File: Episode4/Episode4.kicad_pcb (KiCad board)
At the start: 2 copper layers, 175.3 x 181.6 mm, 64 parts, among them J1 BUS 1, J10 ATX POWER, J2 BUS 2, J3 BUS 3, J4 BUS 4, J5 BUS 5, J6 BUS 6, J7 BUS 7, J8 Conn_02x31_Top_Bottom, J9 Conn_02x18_Top_Bottom, SW1 POWER, U1 74HCT14, U2 74HCT74

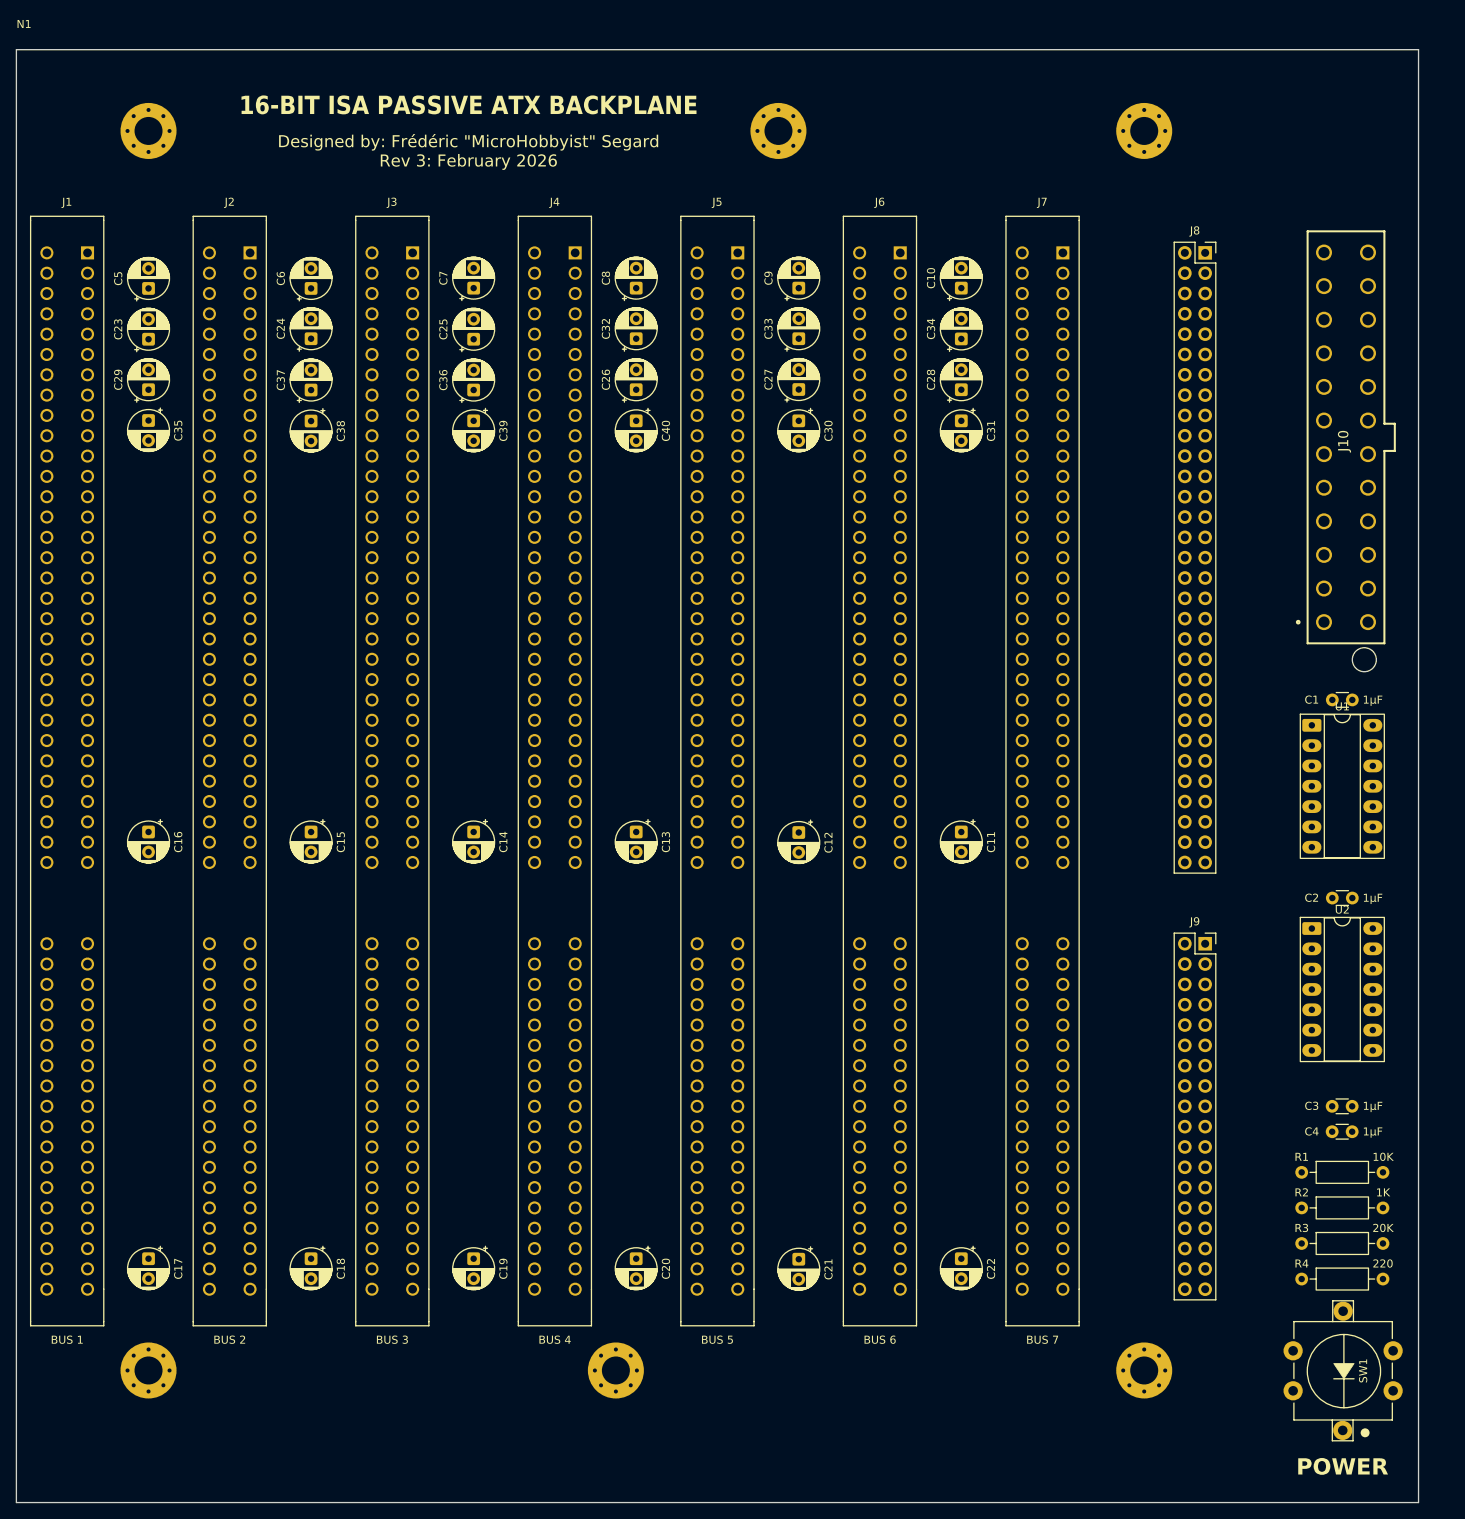
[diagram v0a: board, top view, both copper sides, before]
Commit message: Added traces to the backplane manually.
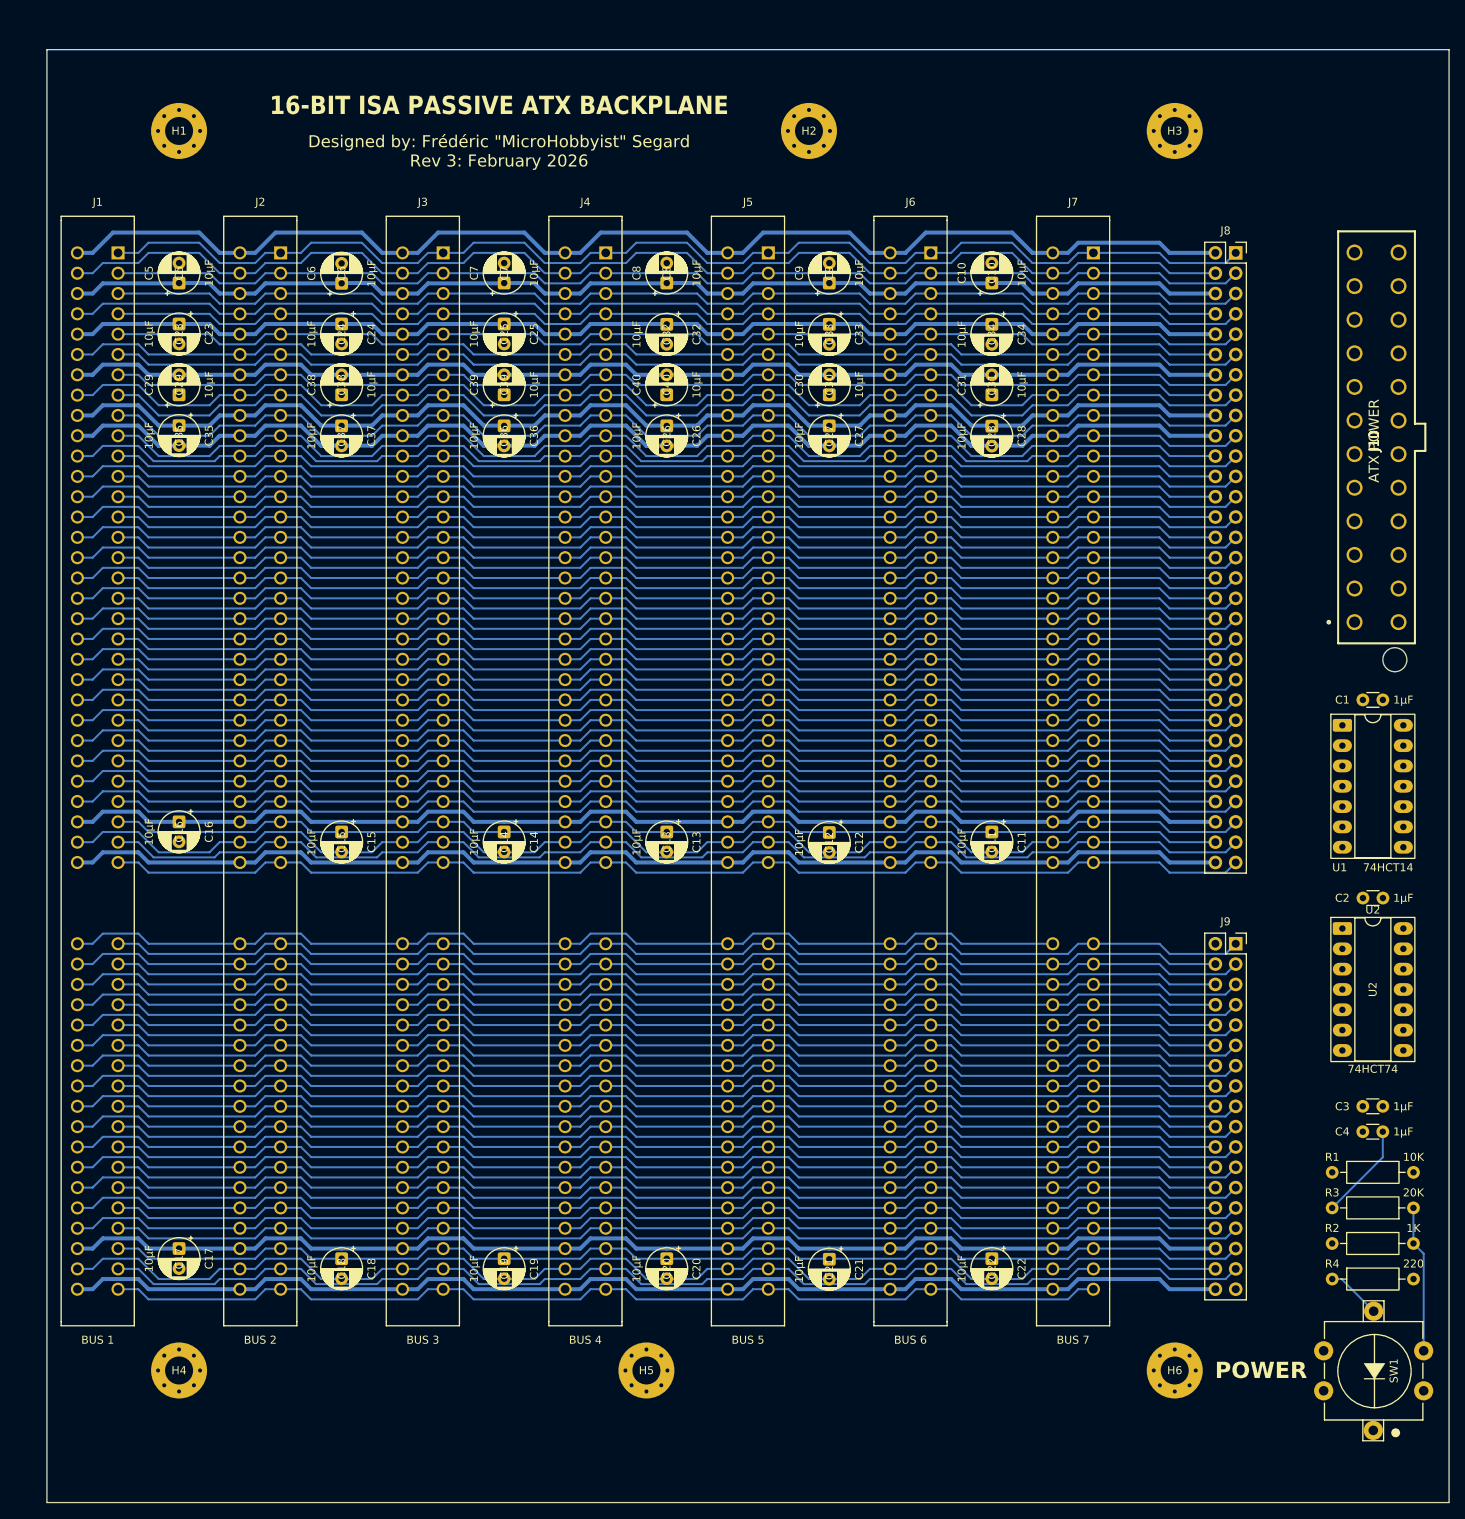
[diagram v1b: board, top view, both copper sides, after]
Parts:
- moved R3 14.7 mm to (200.0, 163.8), turned to 180 degrees
- moved C2 6.33 mm to (196.2, 125.1), turned to 180 degrees
- moved C3 6.33 mm to (196.2, 151.1), turned to 180 degrees
- moved C4 6.33 mm to (196.2, 154.3), turned to 180 degrees
- moved C27 5.93 mm to (127.0, 66.1), turned to -90 degrees
- moved C28 5.93 mm to (147.3, 66.1), turned to -90 degrees
- moved C26 5.92 mm to (106.7, 66.1), turned to -90 degrees
- moved C37 5.88 mm to (66.0, 66.1), turned to -90 degrees
- moved C36 5.88 mm to (86.4, 66.1), turned to -90 degrees
- moved R2 5.85 mm to (189.9, 168.3)
- moved C38 5.03 mm to (66.0, 62.2), turned to 90 degrees
- moved C31 5.02 mm to (147.3, 62.2), turned to 90 degrees
- moved C30 5.02 mm to (127.0, 62.2), turned to 90 degrees
- moved C39 5.02 mm to (86.4, 62.2), turned to 90 degrees
- moved C40 5.01 mm to (106.7, 62.2), turned to 90 degrees
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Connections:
- J1 pad 34: /+5V -> +5V
- J1 pad 36: /+3V3 -> +3V3
- J1 pad 38: /-12V -> -12V
- J1 pad 40: /+12V -> +12V
- J1 pad 60: /+5V -> +5V
- J1 pad 96: /+5V -> +5V
- J2 pad 34: /+5V -> +5V
- J2 pad 36: /+3V3 -> +3V3
- J2 pad 38: /-12V -> -12V
- J2 pad 40: /+12V -> +12V
- J2 pad 60: /+5V -> +5V
- J2 pad 96: /+5V -> +5V
- J3 pad 34: /+5V -> +5V
- J3 pad 36: /+3V3 -> +3V3
- J3 pad 38: /-12V -> -12V
- J3 pad 40: /+12V -> +12V
- J3 pad 60: /+5V -> +5V
- J3 pad 96: /+5V -> +5V
- J4 pad 34: /+5V -> +5V
- J4 pad 36: /+3V3 -> +3V3
- J4 pad 38: /-12V -> -12V
- J4 pad 40: /+12V -> +12V
- J4 pad 60: /+5V -> +5V
- J4 pad 96: /+5V -> +5V
- J5 pad 34: /+5V -> +5V
- J5 pad 36: /+3V3 -> +3V3
- J5 pad 38: /-12V -> -12V
- J5 pad 40: /+12V -> +12V
- J5 pad 60: /+5V -> +5V
- J5 pad 96: /+5V -> +5V
- J6 pad 34: /+5V -> +5V
- J6 pad 36: /+3V3 -> +3V3
- J6 pad 38: /-12V -> -12V
- J6 pad 40: /+12V -> +12V
- J6 pad 60: /+5V -> +5V
- J6 pad 96: /+5V -> +5V
- J7 pad 34: /+5V -> +5V
- J7 pad 36: /+3V3 -> +3V3
- J7 pad 38: /-12V -> -12V
- J7 pad 40: /+12V -> +12V
- J7 pad 60: /+5V -> +5V
- J7 pad 96: /+5V -> +5V
- J8 pad 10: /~{CBLK} -> +3V3
- J8 pad 11: /USR0 -> /D3
- J8 pad 12: /~{MREQ} -> /E
- J8 pad 13: /BA -> /D2
- J8 pad 14: /BS -> -12V
- J8 pad 15: /~{VMA} -> /D1
- J8 pad 16: /A15 -> /Q
- J8 pad 17: /A14 -> /D0
- J8 pad 18: /A13 -> +12V
- J8 pad 19: /A12 -> /~{CBLK}
- J8 pad 2: /D7 -> GND
- J8 pad 20: /A11 -> GND
- J8 pad 21: /A10 -> /USR0
- J8 pad 22: /A9 -> /~{WR}
- J8 pad 23: /A8 -> /~{MREQ}
- J8 pad 24: /A7 -> /~{RD}
- J8 pad 25: /A6 -> /BA
- J8 pad 26: /A5 -> /R/~{W}
- J8 pad 27: /A4 -> /BS
- J8 pad 28: /A3 -> /~{RAM_{oe}}
- J8 pad 29: /A2 -> /~{VMA}
- J8 pad 3: /D6 -> /D7
- J8 pad 30: /A1 -> /MMU_{en}
- J8 pad 31: /A0 -> /A15
- J8 pad 32: GND -> /~{MRDY}
- J8 pad 33: /RESET -> /A14
- J8 pad 34: /+5V -> /~{HALT}
- J8 pad 35: /~{RESET} -> /A13
- J8 pad 36: /+3V3 -> /~{BREQ}
- J8 pad 37: /E -> /A12
- J8 pad 38: /-12V -> /~{NMI}
- J8 pad 39: /Q -> /A11
- J8 pad 4: /D5 -> /RESET
- J8 pad 40: /+12V -> /CLK_{acia}
- J8 pad 41: GND -> /A10
- J8 pad 42: /~{WR} -> /~{IRQ7}
- J8 pad 43: /~{RD} -> /A9
- J8 pad 44: /R/~{W} -> /~{IRQ6}
- J8 pad 45: /~{RAM_{oe}} -> /A8
- J8 pad 46: /MMU_{en} -> /~{IRQ5}
- J8 pad 47: /~{MRDY} -> /A7
- J8 pad 48: /~{HALT} -> /~{IRQ4}
- J8 pad 49: /~{BREQ} -> /A6
- J8 pad 5: /D4 -> /D6
- J8 pad 50: /~{NMI} -> /~{IRQ3}
- J8 pad 51: /CLK_{acia} -> /A5
- J8 pad 52: /~{IRQ7} -> /~{IRQ2}
- J8 pad 53: /~{IRQ6} -> /A4
- J8 pad 54: /~{IRQ5} -> /~{IRQ1}
- J8 pad 55: /~{IRQ4} -> /A3
- J8 pad 56: /~{IRQ3} -> /~{IRQ0}
- J8 pad 57: /~{IRQ2} -> /A2
- J8 pad 58: /~{IRQ1} -> +5V
- J8 pad 59: /~{IRQ0} -> /A1
- J8 pad 6: /D3 -> +5V
- J8 pad 60: /+5V -> /CLK_{cpu}
- J8 pad 61: /CLK_{cpu} -> /A0
- J8 pad 7: /D2 -> /D5
- J8 pad 8: /D1 -> /~{RESET}
- J8 pad 9: /D0 -> /D4
- J9 pad 10: /CLK_{2} -> /~{IRQ12}
- J9 pad 11: /D8 -> /A19
- J9 pad 12: /D9 -> /~{IRQ13}
- J9 pad 13: /D10 -> /A18
- J9 pad 14: /D11 -> /~{IRQ14}
- J9 pad 15: /D12 -> /A17
- J9 pad 16: /D13 -> /~{IRQ15}
- J9 pad 17: /D14 -> /A16
- J9 pad 18: /D15 -> /USR1
- J9 pad 19: /~{IRQ8} -> /CLK_{2}
- J9 pad 2: /A23 -> /~{IRQ8}
- J9 pad 20: /~{IRQ9} -> /USR2
- J9 pad 21: /~{IRQ10} -> /D8
- J9 pad 22: /~{IRQ11} -> /USR3
- J9 pad 23: /~{IRQ12} -> /D9
- J9 pad 24: /~{IRQ13} -> /USR4
- J9 pad 25: /~{IRQ14} -> /D10
- J9 pad 26: /~{IRQ15} -> /USR5
- J9 pad 27: /USR1 -> /D11
- J9 pad 28: /USR2 -> /USR6
- J9 pad 29: /USR3 -> /D12
- J9 pad 3: /A22 -> /A23
- J9 pad 30: /USR4 -> /USR7
- J9 pad 31: /USR5 -> /D13
- J9 pad 32: /USR6 -> +5V
- J9 pad 33: /USR7 -> /D14
- J9 pad 34: /+5V -> /USR8
- J9 pad 35: /USR8 -> /D15
- J9 pad 4: /A21 -> /~{IRQ9}
- J9 pad 5: /A20 -> /A22
- J9 pad 6: /A19 -> /~{IRQ10}
- J9 pad 7: /A18 -> /A21
- J9 pad 8: /A17 -> /~{IRQ11}
- J9 pad 9: /A16 -> /A20
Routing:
- net GND: track 0.00 -> 611.3 mm
- net +5V: track 0.00 -> 449.2 mm
- net /D2: track 0.00 -> 203.6 mm
- net /Q: track 0.00 -> 198.7 mm
- net /RESET: track 0.00 -> 155.9 mm
- net +12V: track 0.00 -> 155.9 mm
- net /D0: track 0.00 -> 153.4 mm
- net /D1: track 0.00 -> 153.4 mm
- net /~{IORQ}: track 0.00 -> 153.4 mm
- net /~{CBLK}: track 0.00 -> 153.4 mm
- net /~{WR}: track 0.00 -> 152.8 mm
- net /D14: track 0.00 -> 150.2 mm
- net /~{IRQ15}: track 0.00 -> 149.6 mm
- net /~{IRQ14}: track 0.00 -> 149.6 mm
- net /~{IRQ12}: track 0.00 -> 149.6 mm
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
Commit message: Added more capacitors and extended the bus form 7 to 12
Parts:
- removed N1: Housing, MicroHobbyist:ATX_Backplane
- added C100: .1µF, Capacitor_THT:C_Disc_D3.4mm_W2.1mm_P2.50mm, F.Cu at (188.3, 170.7)
- added C101: .1µF, Capacitor_THT:C_Disc_D3.4mm_W2.1mm_P2.50mm, F.Cu at (188.3, 174.3)
- added C102: .1µF, Capacitor_THT:C_Disc_D3.4mm_W2.1mm_P2.50mm, F.Cu at (188.3, 178.0)
- added C103: .1µF, Capacitor_THT:C_Disc_D3.4mm_W2.1mm_P2.50mm, F.Cu at (188.3, 181.6)
- added C104: .1µF, Capacitor_THT:C_Disc_D3.4mm_W2.1mm_P2.50mm, F.Cu at (188.3, 185.3)
- added C105: .1µF, Capacitor_THT:C_Disc_D3.4mm_W2.1mm_P2.50mm, F.Cu at (188.3, 188.9)
- added C106: .1µF, Capacitor_THT:C_Disc_D3.4mm_W2.1mm_P2.50mm, F.Cu at (188.3, 192.6)
- added C107: .1µF, Capacitor_THT:C_Disc_D3.4mm_W2.1mm_P2.50mm, F.Cu at (188.3, 196.2)
- added C108: .1µF, Capacitor_THT:C_Disc_D3.4mm_W2.1mm_P2.50mm, F.Cu at (188.3, 199.9)
- added C109: .1µF, Capacitor_THT:C_Disc_D3.4mm_W2.1mm_P2.50mm, F.Cu at (193.9, 152.4)
- added C110: .1µF, Capacitor_THT:C_Disc_D3.4mm_W2.1mm_P2.50mm, F.Cu at (193.9, 156.1)
- added C111: .1µF, Capacitor_THT:C_Disc_D3.4mm_W2.1mm_P2.50mm, F.Cu at (193.9, 159.7)
- added C112: .1µF, Capacitor_THT:C_Disc_D3.4mm_W2.1mm_P2.50mm, F.Cu at (193.9, 163.4)
- added C113: .1µF, Capacitor_THT:C_Disc_D3.4mm_W2.1mm_P2.50mm, F.Cu at (193.9, 167.0)
- added C114: .1µF, Capacitor_THT:C_Disc_D3.4mm_W2.1mm_P2.50mm, F.Cu at (193.9, 170.7)
- added C115: .1µF, Capacitor_THT:C_Disc_D3.4mm_W2.1mm_P2.50mm, F.Cu at (193.9, 174.3)
- added C116: .1µF, Capacitor_THT:C_Disc_D3.4mm_W2.1mm_P2.50mm, F.Cu at (193.9, 178.0)
- added C117: .1µF, Capacitor_THT:C_Disc_D3.4mm_W2.1mm_P2.50mm, F.Cu at (193.9, 181.6)
- added C118: .1µF, Capacitor_THT:C_Disc_D3.4mm_W2.1mm_P2.50mm, F.Cu at (193.9, 185.3)
- added C119: .1µF, Capacitor_THT:C_Disc_D3.4mm_W2.1mm_P2.50mm, F.Cu at (193.9, 188.9)
- added C120: .1µF, Capacitor_THT:C_Disc_D3.4mm_W2.1mm_P2.50mm, F.Cu at (193.9, 192.6)
- added C121: .1µF, Capacitor_THT:C_Disc_D3.4mm_W2.1mm_P2.50mm, F.Cu at (193.9, 196.2)
- added C122: .1µF, Capacitor_THT:C_Disc_D3.4mm_W2.1mm_P2.50mm, F.Cu at (193.9, 199.9)
- added C123: .1µF, Capacitor_THT:C_Disc_D3.4mm_W2.1mm_P2.50mm, F.Cu at (199.6, 152.4)
- added C124: .1µF, Capacitor_THT:C_Disc_D3.4mm_W2.1mm_P2.50mm, F.Cu at (199.6, 156.1)
- added C125: .1µF, Capacitor_THT:C_Disc_D3.4mm_W2.1mm_P2.50mm, F.Cu at (199.6, 159.7)
- added C126: .1µF, Capacitor_THT:C_Disc_D3.4mm_W2.1mm_P2.50mm, F.Cu at (199.6, 163.4)
- added C127: .1µF, Capacitor_THT:C_Disc_D3.4mm_W2.1mm_P2.50mm, F.Cu at (199.6, 167.0)
- added C128: .1µF, Capacitor_THT:C_Disc_D3.4mm_W2.1mm_P2.50mm, F.Cu at (199.6, 170.7)
- added C129: .1µF, Capacitor_THT:C_Disc_D3.4mm_W2.1mm_P2.50mm, F.Cu at (199.6, 174.3)
- added C130: .1µF, Capacitor_THT:C_Disc_D3.4mm_W2.1mm_P2.50mm, F.Cu at (199.6, 178.0)
- added C131: 1µF, Capacitor_THT:C_Disc_D3.4mm_W2.1mm_P2.50mm, F.Cu at (199.6, 181.6)
- added C132: 1µF, Capacitor_THT:C_Disc_D3.4mm_W2.1mm_P2.50mm, F.Cu at (199.6, 185.3)
- added C133: 1µF, Capacitor_THT:C_Disc_D3.4mm_W2.1mm_P2.50mm, F.Cu at (199.6, 188.9)
- added C134: 1µF, Capacitor_THT:C_Disc_D3.4mm_W2.1mm_P2.50mm, F.Cu at (199.6, 192.6)
- added C135: 1µF, Capacitor_THT:C_Disc_D3.4mm_W2.1mm_P2.50mm, F.Cu at (199.6, 196.2)
- added C136: 1µF, Capacitor_THT:C_Disc_D3.4mm_W2.1mm_P2.50mm, F.Cu at (199.6, 199.9)
- added C137: 1µF, Capacitor_THT:C_Disc_D3.4mm_W2.1mm_P2.50mm, F.Cu at (205.2, 152.4)
- added C138: 1µF, Capacitor_THT:C_Disc_D3.4mm_W2.1mm_P2.50mm, F.Cu at (205.2, 156.1)
- added C139: 1µF, Capacitor_THT:C_Disc_D3.4mm_W2.1mm_P2.50mm, F.Cu at (205.2, 159.7)
- added C140: 1µF, Capacitor_THT:C_Disc_D3.4mm_W2.1mm_P2.50mm, F.Cu at (205.2, 163.4)
- added C141: 1µF, Capacitor_THT:C_Disc_D3.4mm_W2.1mm_P2.50mm, F.Cu at (205.2, 167.0)
- added C142: .1µF, Capacitor_THT:C_Disc_D3.4mm_W2.1mm_P2.50mm, F.Cu at (205.2, 170.7)
- added C143: .1µF, Capacitor_THT:C_Disc_D3.4mm_W2.1mm_P2.50mm, F.Cu at (205.2, 174.3)
- added C144: .1µF, Capacitor_THT:C_Disc_D3.4mm_W2.1mm_P2.50mm, F.Cu at (205.2, 178.0)
- added C145: .1µF, Capacitor_THT:C_Disc_D3.4mm_W2.1mm_P2.50mm, F.Cu at (205.2, 181.6)
- added C146: .1µF, Capacitor_THT:C_Disc_D3.4mm_W2.1mm_P2.50mm, F.Cu at (205.2, 185.3)
- added C147: .1µF, Capacitor_THT:C_Disc_D3.4mm_W2.1mm_P2.50mm, F.Cu at (205.2, 188.9)
- added C148: .1µF, Capacitor_THT:C_Disc_D3.4mm_W2.1mm_P2.50mm, F.Cu at (205.2, 192.6)
- added C149: .1µF, Capacitor_THT:C_Disc_D3.4mm_W2.1mm_P2.50mm, F.Cu at (205.2, 196.2)
- added C150: .1µF, Capacitor_THT:C_Disc_D3.4mm_W2.1mm_P2.50mm, F.Cu at (205.2, 199.9)
- added C151: .1µF, Capacitor_THT:C_Disc_D3.4mm_W2.1mm_P2.50mm, F.Cu at (210.9, 152.4)
- added C152: .1µF, Capacitor_THT:C_Disc_D3.4mm_W2.1mm_P2.50mm, F.Cu at (210.9, 156.1)
- added C153: 1µF, Capacitor_THT:C_Disc_D3.4mm_W2.1mm_P2.50mm, F.Cu at (210.9, 159.7)
- added C154: 1µF, Capacitor_THT:C_Disc_D3.4mm_W2.1mm_P2.50mm, F.Cu at (210.9, 163.4)
- added C155: 1µF, Capacitor_THT:C_Disc_D3.4mm_W2.1mm_P2.50mm, F.Cu at (210.9, 167.0)
- added C156: 1µF, Capacitor_THT:C_Disc_D3.4mm_W2.1mm_P2.50mm, F.Cu at (210.9, 170.7)
- added C157: 1µF, Capacitor_THT:C_Disc_D3.4mm_W2.1mm_P2.50mm, F.Cu at (210.9, 174.3)
- added C158: 1µF, Capacitor_THT:C_Disc_D3.4mm_W2.1mm_P2.50mm, F.Cu at (210.9, 178.0)
- added C159: 1µF, Capacitor_THT:C_Disc_D3.4mm_W2.1mm_P2.50mm, F.Cu at (210.9, 181.6)
- added C160: 1µF, Capacitor_THT:C_Disc_D3.4mm_W2.1mm_P2.50mm, F.Cu at (210.9, 185.3)
- added C161: 1µF, Capacitor_THT:C_Disc_D3.4mm_W2.1mm_P2.50mm, F.Cu at (210.9, 188.9)
- added C162: 1µF, Capacitor_THT:C_Disc_D3.4mm_W2.1mm_P2.50mm, F.Cu at (210.9, 192.6)
- added C163: 1µF, Capacitor_THT:C_Disc_D3.4mm_W2.1mm_P2.50mm, F.Cu at (210.9, 196.2)
- added C164: .1µF, Capacitor_THT:C_Disc_D3.4mm_W2.1mm_P2.50mm, F.Cu at (210.9, 199.9)
- added C165: .1µF, Capacitor_THT:C_Disc_D3.4mm_W2.1mm_P2.50mm, F.Cu at (216.5, 152.4)
- added C166: .1µF, Capacitor_THT:C_Disc_D3.4mm_W2.1mm_P2.50mm, F.Cu at (216.5, 156.1)
- added C167: .1µF, Capacitor_THT:C_Disc_D3.4mm_W2.1mm_P2.50mm, F.Cu at (216.5, 159.7)
- added C168: .1µF, Capacitor_THT:C_Disc_D3.4mm_W2.1mm_P2.50mm, F.Cu at (216.5, 163.4)
- added C169: .1µF, Capacitor_THT:C_Disc_D3.4mm_W2.1mm_P2.50mm, F.Cu at (216.5, 167.0)
- added C170: .1µF, Capacitor_THT:C_Disc_D3.4mm_W2.1mm_P2.50mm, F.Cu at (216.5, 170.7)
- added C171: .1µF, Capacitor_THT:C_Disc_D3.4mm_W2.1mm_P2.50mm, F.Cu at (216.5, 174.3)
- added C172: .1µF, Capacitor_THT:C_Disc_D3.4mm_W2.1mm_P2.50mm, F.Cu at (216.5, 178.0)
- added C173: .1µF, Capacitor_THT:C_Disc_D3.4mm_W2.1mm_P2.50mm, F.Cu at (216.5, 181.6)
- added C174: .1µF, Capacitor_THT:C_Disc_D3.4mm_W2.1mm_P2.50mm, F.Cu at (216.5, 185.3)
- added C41: 10µF, Capacitor_THT:CP_Radial_D5.0mm_P2.50mm, F.Cu at (145.3, 180.1)
- added C42: 10µF, Capacitor_THT:CP_Radial_D5.0mm_P2.50mm, F.Cu at (145.3, 186.6)
- added C43: 10µF, Capacitor_THT:CP_Radial_D5.0mm_P2.50mm, F.Cu at (145.3, 193.2)
- added C44: 10µF, Capacitor_THT:CP_Radial_D5.0mm_P2.50mm, F.Cu at (145.3, 199.7)
- added C45: 10µF, Capacitor_THT:CP_Radial_D5.0mm_P2.50mm, F.Cu at (151.9, 153.9)
- added C46: 10µF, Capacitor_THT:CP_Radial_D5.0mm_P2.50mm, F.Cu at (151.9, 160.4)
- added C47: 10µF, Capacitor_THT:CP_Radial_D5.0mm_P2.50mm, F.Cu at (151.9, 167.0)
- added C48: 10µF, Capacitor_THT:CP_Radial_D5.0mm_P2.50mm, F.Cu at (151.9, 173.5)
- added C49: 10µF, Capacitor_THT:CP_Radial_D5.0mm_P2.50mm, F.Cu at (151.9, 180.1)
- added C50: 10µF, Capacitor_THT:CP_Radial_D5.0mm_P2.50mm, F.Cu at (151.9, 186.6)
- added C51: 10µF, Capacitor_THT:CP_Radial_D5.0mm_P2.50mm, F.Cu at (151.9, 193.2)
- added C52: 10µF, Capacitor_THT:CP_Radial_D5.0mm_P2.50mm, F.Cu at (151.9, 199.7)
- added C53: 10µF, Capacitor_THT:CP_Radial_D5.0mm_P2.50mm, F.Cu at (158.6, 153.9)
- added C54: 10µF, Capacitor_THT:CP_Radial_D5.0mm_P2.50mm, F.Cu at (158.6, 160.4)
- added C55: 10µF, Capacitor_THT:CP_Radial_D5.0mm_P2.50mm, F.Cu at (158.6, 167.0)
- added C56: 10µF, Capacitor_THT:CP_Radial_D5.0mm_P2.50mm, F.Cu at (158.6, 173.5)
- added C57: 10µF, Capacitor_THT:CP_Radial_D5.0mm_P2.50mm, F.Cu at (158.6, 180.1)
- added C58: 10µF, Capacitor_THT:CP_Radial_D5.0mm_P2.50mm, F.Cu at (158.6, 186.6)
- added C59: 10µF, Capacitor_THT:CP_Radial_D5.0mm_P2.50mm, F.Cu at (158.6, 193.2)
- added C60: 10µF, Capacitor_THT:CP_Radial_D5.0mm_P2.50mm, F.Cu at (158.6, 199.7)
- added C61: 10µF, Capacitor_THT:CP_Radial_D5.0mm_P2.50mm, F.Cu at (165.2, 153.9)
- added C62: 10µF, Capacitor_THT:CP_Radial_D5.0mm_P2.50mm, F.Cu at (165.2, 160.4)
- added C63: 10µF, Capacitor_THT:CP_Radial_D5.0mm_P2.50mm, F.Cu at (165.2, 167.0)
- added C64: 10µF, Capacitor_THT:CP_Radial_D5.0mm_P2.50mm, F.Cu at (165.2, 173.5)
- added C65: 1µF, Capacitor_THT:C_Disc_D3.4mm_W2.1mm_P2.50mm, F.Cu at (171.3, 196.2)
- added C66: 1µF, Capacitor_THT:C_Disc_D3.4mm_W2.1mm_P2.50mm, F.Cu at (171.3, 199.9)
- added C67: 1µF, Capacitor_THT:C_Disc_D3.4mm_W2.1mm_P2.50mm, F.Cu at (177.0, 152.4)
- added C68: 1µF, Capacitor_THT:C_Disc_D3.4mm_W2.1mm_P2.50mm, F.Cu at (177.0, 156.1)
- added C69: 1µF, Capacitor_THT:C_Disc_D3.4mm_W2.1mm_P2.50mm, F.Cu at (177.0, 159.7)
- added C70: 1µF, Capacitor_THT:C_Disc_D3.4mm_W2.1mm_P2.50mm, F.Cu at (177.0, 163.4)
- added C71: 1µF, Capacitor_THT:C_Disc_D3.4mm_W2.1mm_P2.50mm, F.Cu at (177.0, 167.0)
- added C72: 1µF, Capacitor_THT:C_Disc_D3.4mm_W2.1mm_P2.50mm, F.Cu at (177.0, 170.7)
- added C73: 1µF, Capacitor_THT:C_Disc_D3.4mm_W2.1mm_P2.50mm, F.Cu at (177.0, 174.3)
- added C74: 1µF, Capacitor_THT:C_Disc_D3.4mm_W2.1mm_P2.50mm, F.Cu at (177.0, 178.0)
- added C75: 1µF, Capacitor_THT:C_Disc_D3.4mm_W2.1mm_P2.50mm, F.Cu at (177.0, 181.6)
- added C76: 1µF, Capacitor_THT:C_Disc_D3.4mm_W2.1mm_P2.50mm, F.Cu at (177.0, 185.3)
- added C77: 1µF, Capacitor_THT:C_Disc_D3.4mm_W2.1mm_P2.50mm, F.Cu at (177.0, 188.9)
- added C78: 1µF, Capacitor_THT:C_Disc_D3.4mm_W2.1mm_P2.50mm, F.Cu at (177.0, 192.6)
- added C79: 1µF, Capacitor_THT:C_Disc_D3.4mm_W2.1mm_P2.50mm, F.Cu at (177.0, 196.2)
- added C80: 1µF, Capacitor_THT:C_Disc_D3.4mm_W2.1mm_P2.50mm, F.Cu at (177.0, 199.9)
- added C81: 1µF, Capacitor_THT:C_Disc_D3.4mm_W2.1mm_P2.50mm, F.Cu at (182.6, 152.4)
- added C82: 1µF, Capacitor_THT:C_Disc_D3.4mm_W2.1mm_P2.50mm, F.Cu at (182.6, 156.1)
- added C83: 1µF, Capacitor_THT:C_Disc_D3.4mm_W2.1mm_P2.50mm, F.Cu at (182.6, 159.7)
- added C84: 1µF, Capacitor_THT:C_Disc_D3.4mm_W2.1mm_P2.50mm, F.Cu at (182.6, 163.4)
- added C85: 1µF, Capacitor_THT:C_Disc_D3.4mm_W2.1mm_P2.50mm, F.Cu at (182.6, 167.0)
- added C86: 1µF, Capacitor_THT:C_Disc_D3.4mm_W2.1mm_P2.50mm, F.Cu at (182.6, 170.7)
- added C87: 1µF, Capacitor_THT:C_Disc_D3.4mm_W2.1mm_P2.50mm, F.Cu at (182.6, 174.3)
- added C88: 1µF, Capacitor_THT:C_Disc_D3.4mm_W2.1mm_P2.50mm, F.Cu at (182.6, 178.0)
- added C89: 1µF, Capacitor_THT:C_Disc_D3.4mm_W2.1mm_P2.50mm, F.Cu at (182.6, 181.6)
- added C90: 1µF, Capacitor_THT:C_Disc_D3.4mm_W2.1mm_P2.50mm, F.Cu at (182.6, 185.3)
- added C91: 1µF, Capacitor_THT:C_Disc_D3.4mm_W2.1mm_P2.50mm, F.Cu at (182.6, 188.9)
- added C92: 1µF, Capacitor_THT:C_Disc_D3.4mm_W2.1mm_P2.50mm, F.Cu at (182.6, 192.6)
- added C93: 1µF, Capacitor_THT:C_Disc_D3.4mm_W2.1mm_P2.50mm, F.Cu at (182.6, 196.2)
- added C94: 1µF, Capacitor_THT:C_Disc_D3.4mm_W2.1mm_P2.50mm, F.Cu at (182.6, 199.9)
- added C95: 1µF, Capacitor_THT:C_Disc_D3.4mm_W2.1mm_P2.50mm, F.Cu at (188.3, 152.4)
- added C96: 1µF, Capacitor_THT:C_Disc_D3.4mm_W2.1mm_P2.50mm, F.Cu at (188.3, 156.1)
- added C97: 1µF, Capacitor_THT:C_Disc_D3.4mm_W2.1mm_P2.50mm, F.Cu at (188.3, 159.7)
- added C98: .1µF, Capacitor_THT:C_Disc_D3.4mm_W2.1mm_P2.50mm, F.Cu at (188.3, 163.4)
- added C99: .1µF, Capacitor_THT:C_Disc_D3.4mm_W2.1mm_P2.50mm, F.Cu at (188.3, 167.0)
- added H10: MH, MountingHole:MountingHole_3.5mm_Pad_Via, F.Cu at (94.0, 31.8)
- added H7: MH, MountingHole:MountingHole_3.5mm_Pad_Via, F.Cu at (276.9, 31.8)
- added H8: MH, MountingHole:MountingHole_3.5mm_Pad_Via, F.Cu at (215.9, 31.8)
- added H9: MH, MountingHole:MountingHole_3.5mm_Pad_Via, F.Cu at (154.9, 31.8)
- added J10: BUS 10, MicroHobbyist:ISA_Connector, F.Cu at (238.8, 44.5)
- added J11: BUS 11, MicroHobbyist:ISA_Connector, F.Cu at (259.1, 44.5)
- added J12: BUS 12, MicroHobbyist:ISA_Connector, F.Cu at (279.4, 44.5)
- added J8: BUS 8, MicroHobbyist:ISA_Connector, F.Cu at (198.1, 44.5)
- C1: renamed from C3; footprint Capacitor_THT:C_Disc_D3.0mm_W1.6mm_P2.50mm -> Capacitor_THT:C_Disc_D3.4mm_W2.1mm_P2.50mm
- C10, C13, C14, C17, C20, C7, C8, C9: value 10µF -> .1µF; footprint Capacitor_THT:CP_Radial_D5.0mm_P2.50mm -> Capacitor_THT:C_Disc_D3.4mm_W2.1mm_P2.50mm
- C11, C15, C18, C5: value 10µF -> 100µF; footprint Capacitor_THT:CP_Radial_D5.0mm_P2.50mm -> Capacitor_THT:CP_Radial_D6.3mm_P2.50mm
- C12, C16, C19, C6: value 10µF -> 1µF; footprint Capacitor_THT:CP_Radial_D5.0mm_P2.50mm -> Capacitor_THT:C_Disc_D3.4mm_W2.1mm_P2.50mm
- C2: renamed from C4; footprint Capacitor_THT:C_Disc_D3.0mm_W1.6mm_P2.50mm -> Capacitor_THT:C_Disc_D3.4mm_W2.1mm_P2.50mm
- C3: renamed from C1; value 1µF -> .1µF; footprint Capacitor_THT:C_Disc_D3.0mm_W1.6mm_P2.50mm -> Capacitor_THT:C_Disc_D3.4mm_W2.1mm_P2.50mm
- C4: renamed from C2; value 1µF -> .1µF; footprint Capacitor_THT:C_Disc_D3.0mm_W1.6mm_P2.50mm -> Capacitor_THT:C_Disc_D3.4mm_W2.1mm_P2.50mm
- J1, J2, J3, J4, J5, J6, J7: footprint MicroHobbyist:ISA_Connector_98 -> MicroHobbyist:ISA_Connector
- J9: value Conn_02x18_Top_Bottom -> BUS 9; footprint Connector_PinSocket_2.54mm:PinSocket_2x18_P2.54mm_Vertical -> MicroHobbyist:ISA_Connector
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- renumbered J8 to J13, J10 to J14
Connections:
- C11 pad 1: +5V -> +3V3
- C12 pad 1: +5V -> +3V3
- C13 pad 1: +5V -> +3V3
- C14 pad 1: +5V -> +3V3
- C15 pad 1: +5V -> +12V
- C16 pad 1: +5V -> +12V
- C17 pad 1: +5V -> +12V
- C18 pad 1: +5V -> GND
- C18 pad 2: GND -> -12V
- C19 pad 1: +5V -> -12V
- C20 pad 1: +5V -> -12V
- C23 pad 1: +3V3 -> +5V
- C24 pad 1: +3V3 -> +5V
- C25 pad 1: +3V3 -> +5V
- C26 pad 1: +12V -> +5V
- C27 pad 1: +12V -> +5V
- C28 pad 1: +12V -> +5V
- C29 pad 1: GND -> +5V
- C29 pad 2: -12V -> GND
- C30 pad 1: GND -> +5V
- C30 pad 2: -12V -> GND
- C31 pad 1: GND -> +5V
- C31 pad 2: -12V -> GND
- C32 pad 1: +3V3 -> +5V
- C33 pad 1: +3V3 -> +5V
- C34 pad 1: +3V3 -> +5V
- C35 pad 1: +12V -> +5V
- C36 pad 1: +12V -> +5V
- C37 pad 1: +12V -> +5V
- C38 pad 1: GND -> +5V
- C38 pad 2: -12V -> GND
- C39 pad 1: GND -> +5V
- C39 pad 2: -12V -> GND
- C40 pad 1: GND -> +5V
- C40 pad 2: -12V -> GND
- J1 pad 1: /~{IORQ} -> /A0
- J1 pad 10: /~{CBLK} -> /A9
- J1 pad 11: /USR0 -> /A10
- J1 pad 12: /~{MREQ} -> /A11
- J1 pad 13: /BA -> /A12
- J1 pad 14: /BS -> /A13
- J1 pad 15: /~{VMA} -> /A14
- J1 pad 17: /A14 -> GND
- J1 pad 18: /A13 -> -12V
- J1 pad 19: /A12 -> +12V
- J1 pad 2: /D7 -> /A1
- J1 pad 20: /A11 -> GND
- J1 pad 21: /A10 -> +3V3
- J1 pad 22: /A9 -> +3V3
- J1 pad 23: /A8 -> GND
- J1 pad 24: /A7 -> /D0
- J1 pad 25: /A6 -> /D1
- J1 pad 26: /A5 -> /D2
- J1 pad 27: /A4 -> /D3
- J1 pad 28: /A3 -> /D4
- J1 pad 29: /A2 -> /D5
- J1 pad 3: /D6 -> /A2
- J1 pad 30: /A1 -> /D6
- J1 pad 31: /A0 -> /D7
- J1 pad 33: /RESET -> +5V
- J1 pad 35: /~{RESET} -> GND
- J1 pad 36: +3V3 -> /E
- J1 pad 37: /E -> /Q
- J1 pad 38: -12V -> /~{VMA}
- J1 pad 39: /Q -> GND
- J1 pad 4: /D5 -> /A3
- J1 pad 40: +12V -> /R/~{W}
- J1 pad 41: GND -> /~{RD}
- J1 pad 43: /~{RD} -> /~{RAM_{oe}}
- J1 pad 44: /R/~{W} -> GND
- J1 pad 45: /~{RAM_{oe}} -> /~{CBLK}
- J1 pad 46: /MMU_{en} -> /~{IORQ}
- J1 pad 47: /~{MRDY} -> /~{MREQ}
- J1 pad 49: /~{BREQ} -> /~{MRDY}
- J1 pad 5: /D4 -> /A4
- J1 pad 50: /~{NMI} -> /~{BREQ}
- J1 pad 51: /CLK_{acia} -> GND
- J1 pad 52: /~{IRQ7} -> /BA
- J1 pad 53: /~{IRQ6} -> /BS
- J1 pad 54: /~{IRQ5} -> /SPARE
- J1 pad 55: /~{IRQ4} -> /~{RESET}
- J1 pad 56: /~{IRQ3} -> /~{NMI}
- J1 pad 57: /~{IRQ2} -> /~{IRQ}
- J1 pad 58: /~{IRQ1} -> /~{FIRQ}
- J1 pad 59: /~{IRQ0} -> GND
- J1 pad 6: /D3 -> /A5
- J1 pad 61: /CLK_{cpu} -> +5V
- J1 pad 7: /D2 -> /A6
- J1 pad 8: /D1 -> /A7
- J1 pad 9: /D0 -> /A8
- J13 pad 1: /~{IORQ} -> /A0
- J13 pad 10: +3V3 -> /E
- J13 pad 11: /D3 -> /A5
- J13 pad 12: /E -> /Q
- J13 pad 13: /D2 -> /A6
- J13 pad 14: -12V -> /~{VMA}
- J13 pad 15: /D1 -> /A7
- J13 pad 16: /Q -> GND
- J13 pad 17: /D0 -> /A8
- J13 pad 18: +12V -> /R/~{W}
- J13 pad 19: /~{CBLK} -> /A9
- J13 pad 20: GND -> /~{RD}
- J13 pad 21: /USR0 -> /A10
- J13 pad 23: /~{MREQ} -> /A11
- J13 pad 24: /~{RD} -> /~{RAM_{oe}}
- J13 pad 25: /BA -> /A12
- J13 pad 26: /R/~{W} -> GND
- J13 pad 27: /BS -> /A13
- J13 pad 28: /~{RAM_{oe}} -> /~{CBLK}
- J13 pad 29: /~{VMA} -> /A14
- J13 pad 3: /D7 -> /A1
- J13 pad 30: /MMU_{en} -> /~{IORQ}
- J13 pad 32: /~{MRDY} -> /~{MREQ}
- J13 pad 33: /A14 -> GND
- J13 pad 35: /A13 -> -12V
- J13 pad 36: /~{BREQ} -> /~{MRDY}
- J13 pad 37: /A12 -> +12V
- J13 pad 38: /~{NMI} -> /~{BREQ}
- J13 pad 39: /A11 -> GND
- J13 pad 4: /RESET -> +5V
- J13 pad 40: /CLK_{acia} -> GND
- J13 pad 41: /A10 -> +3V3
- J13 pad 42: /~{IRQ7} -> /BA
- J13 pad 43: /A9 -> +3V3
- J13 pad 44: /~{IRQ6} -> /BS
- J13 pad 45: /A8 -> GND
- J13 pad 46: /~{IRQ5} -> /SPARE
- J13 pad 47: /A7 -> /D0
- J13 pad 48: /~{IRQ4} -> /~{RESET}
- J13 pad 49: /A6 -> /D1
- J13 pad 5: /D6 -> /A2
- J13 pad 50: /~{IRQ3} -> /~{NMI}
- J13 pad 51: /A5 -> /D2
- J13 pad 52: /~{IRQ2} -> /~{IRQ}
- J13 pad 53: /A4 -> /D3
- J13 pad 54: /~{IRQ1} -> /~{FIRQ}
- J13 pad 55: /A3 -> /D4
- J13 pad 56: /~{IRQ0} -> GND
- J13 pad 57: /A2 -> /D5
- J13 pad 59: /A1 -> /D6
- J13 pad 60: /CLK_{cpu} -> +5V
- J13 pad 61: /A0 -> /D7
- J13 pad 7: /D5 -> /A3
- J13 pad 8: /~{RESET} -> GND
- J13 pad 9: /D4 -> /A4
- J2 pad 1: /~{IORQ} -> /A0
- J2 pad 10: /~{CBLK} -> /A9
- J2 pad 11: /USR0 -> /A10
- J2 pad 12: /~{MREQ} -> /A11
- J2 pad 13: /BA -> /A12
- J2 pad 14: /BS -> /A13
- J2 pad 15: /~{VMA} -> /A14
- J2 pad 17: /A14 -> GND
- J2 pad 18: /A13 -> -12V
- J2 pad 19: /A12 -> +12V
- J2 pad 2: /D7 -> /A1
- J2 pad 20: /A11 -> GND
- J2 pad 21: /A10 -> +3V3
- J2 pad 22: /A9 -> +3V3
- J2 pad 23: /A8 -> GND
- J2 pad 24: /A7 -> /D0
- J2 pad 25: /A6 -> /D1
- J2 pad 26: /A5 -> /D2
- J2 pad 27: /A4 -> /D3
- J2 pad 28: /A3 -> /D4
- J2 pad 29: /A2 -> /D5
- J2 pad 3: /D6 -> /A2
- J2 pad 30: /A1 -> /D6
- J2 pad 31: /A0 -> /D7
- J2 pad 33: /RESET -> +5V
- J2 pad 35: /~{RESET} -> GND
- J2 pad 36: +3V3 -> /E
- J2 pad 37: /E -> /Q
- J2 pad 38: -12V -> /~{VMA}
- J2 pad 39: /Q -> GND
- J2 pad 4: /D5 -> /A3
- J2 pad 40: +12V -> /R/~{W}
- J2 pad 41: GND -> /~{RD}
- J2 pad 43: /~{RD} -> /~{RAM_{oe}}
- J2 pad 44: /R/~{W} -> GND
- J2 pad 45: /~{RAM_{oe}} -> /~{CBLK}
- J2 pad 46: /MMU_{en} -> /~{IORQ}
- J2 pad 47: /~{MRDY} -> /~{MREQ}
- J2 pad 49: /~{BREQ} -> /~{MRDY}
- J2 pad 5: /D4 -> /A4
- J2 pad 50: /~{NMI} -> /~{BREQ}
- J2 pad 51: /CLK_{acia} -> GND
- J2 pad 52: /~{IRQ7} -> /BA
- J2 pad 53: /~{IRQ6} -> /BS
- J2 pad 54: /~{IRQ5} -> /SPARE
- J2 pad 55: /~{IRQ4} -> /~{RESET}
- J2 pad 56: /~{IRQ3} -> /~{NMI}
- J2 pad 57: /~{IRQ2} -> /~{IRQ}
- J2 pad 58: /~{IRQ1} -> /~{FIRQ}
- J2 pad 59: /~{IRQ0} -> GND
- J2 pad 6: /D3 -> /A5
- J2 pad 61: /CLK_{cpu} -> +5V
- J2 pad 7: /D2 -> /A6
- J2 pad 8: /D1 -> /A7
- J2 pad 9: /D0 -> /A8
- J3 pad 1: /~{IORQ} -> /A0
- J3 pad 10: /~{CBLK} -> /A9
- J3 pad 11: /USR0 -> /A10
- J3 pad 12: /~{MREQ} -> /A11
- J3 pad 13: /BA -> /A12
- J3 pad 14: /BS -> /A13
- J3 pad 15: /~{VMA} -> /A14
- J3 pad 17: /A14 -> GND
- J3 pad 18: /A13 -> -12V
- J3 pad 19: /A12 -> +12V
- J3 pad 2: /D7 -> /A1
- J3 pad 20: /A11 -> GND
- J3 pad 21: /A10 -> +3V3
- J3 pad 22: /A9 -> +3V3
- J3 pad 23: /A8 -> GND
- J3 pad 24: /A7 -> /D0
- J3 pad 25: /A6 -> /D1
- J3 pad 26: /A5 -> /D2
- J3 pad 27: /A4 -> /D3
- J3 pad 28: /A3 -> /D4
- J3 pad 29: /A2 -> /D5
- J3 pad 3: /D6 -> /A2
- J3 pad 30: /A1 -> /D6
- J3 pad 31: /A0 -> /D7
- J3 pad 33: /RESET -> +5V
- J3 pad 35: /~{RESET} -> GND
- J3 pad 36: +3V3 -> /E
- J3 pad 37: /E -> /Q
- J3 pad 38: -12V -> /~{VMA}
- J3 pad 39: /Q -> GND
- J3 pad 4: /D5 -> /A3
- J3 pad 40: +12V -> /R/~{W}
- J3 pad 41: GND -> /~{RD}
- J3 pad 43: /~{RD} -> /~{RAM_{oe}}
- J3 pad 44: /R/~{W} -> GND
- J3 pad 45: /~{RAM_{oe}} -> /~{CBLK}
- J3 pad 46: /MMU_{en} -> /~{IORQ}
- J3 pad 47: /~{MRDY} -> /~{MREQ}
- J3 pad 49: /~{BREQ} -> /~{MRDY}
- J3 pad 5: /D4 -> /A4
- J3 pad 50: /~{NMI} -> /~{BREQ}
- J3 pad 51: /CLK_{acia} -> GND
- J3 pad 52: /~{IRQ7} -> /BA
- J3 pad 53: /~{IRQ6} -> /BS
- J3 pad 54: /~{IRQ5} -> /SPARE
- J3 pad 55: /~{IRQ4} -> /~{RESET}
- J3 pad 56: /~{IRQ3} -> /~{NMI}
- J3 pad 57: /~{IRQ2} -> /~{IRQ}
- J3 pad 58: /~{IRQ1} -> /~{FIRQ}
- J3 pad 59: /~{IRQ0} -> GND
- J3 pad 6: /D3 -> /A5
- J3 pad 61: /CLK_{cpu} -> +5V
- J3 pad 7: /D2 -> /A6
- J3 pad 8: /D1 -> /A7
- J3 pad 9: /D0 -> /A8
- J4 pad 1: /~{IORQ} -> /A0
- J4 pad 10: /~{CBLK} -> /A9
- J4 pad 11: /USR0 -> /A10
- J4 pad 12: /~{MREQ} -> /A11
- J4 pad 13: /BA -> /A12
- J4 pad 14: /BS -> /A13
- J4 pad 15: /~{VMA} -> /A14
- J4 pad 17: /A14 -> GND
- J4 pad 18: /A13 -> -12V
- J4 pad 19: /A12 -> +12V
- J4 pad 2: /D7 -> /A1
- J4 pad 20: /A11 -> GND
- J4 pad 21: /A10 -> +3V3
- J4 pad 22: /A9 -> +3V3
- J4 pad 23: /A8 -> GND
- J4 pad 24: /A7 -> /D0
- J4 pad 25: /A6 -> /D1
- J4 pad 26: /A5 -> /D2
- J4 pad 27: /A4 -> /D3
- J4 pad 28: /A3 -> /D4
- J4 pad 29: /A2 -> /D5
- J4 pad 3: /D6 -> /A2
- J4 pad 30: /A1 -> /D6
- J4 pad 31: /A0 -> /D7
- J4 pad 33: /RESET -> +5V
- J4 pad 35: /~{RESET} -> GND
- J4 pad 36: +3V3 -> /E
- J4 pad 37: /E -> /Q
- J4 pad 38: -12V -> /~{VMA}
- J4 pad 39: /Q -> GND
- J4 pad 4: /D5 -> /A3
- J4 pad 40: +12V -> /R/~{W}
- J4 pad 41: GND -> /~{RD}
- J4 pad 43: /~{RD} -> /~{RAM_{oe}}
- J4 pad 44: /R/~{W} -> GND
- J4 pad 45: /~{RAM_{oe}} -> /~{CBLK}
- J4 pad 46: /MMU_{en} -> /~{IORQ}
- J4 pad 47: /~{MRDY} -> /~{MREQ}
- J4 pad 49: /~{BREQ} -> /~{MRDY}
- J4 pad 5: /D4 -> /A4
- J4 pad 50: /~{NMI} -> /~{BREQ}
- J4 pad 51: /CLK_{acia} -> GND
- J4 pad 52: /~{IRQ7} -> /BA
- J4 pad 53: /~{IRQ6} -> /BS
- J4 pad 54: /~{IRQ5} -> /SPARE
- J4 pad 55: /~{IRQ4} -> /~{RESET}
- J4 pad 56: /~{IRQ3} -> /~{NMI}
- J4 pad 57: /~{IRQ2} -> /~{IRQ}
- J4 pad 58: /~{IRQ1} -> /~{FIRQ}
- J4 pad 59: /~{IRQ0} -> GND
- J4 pad 6: /D3 -> /A5
- J4 pad 61: /CLK_{cpu} -> +5V
- J4 pad 7: /D2 -> /A6
- J4 pad 8: /D1 -> /A7
- J4 pad 9: /D0 -> /A8
- J5 pad 1: /~{IORQ} -> /A0
- J5 pad 10: /~{CBLK} -> /A9
- J5 pad 11: /USR0 -> /A10
- J5 pad 12: /~{MREQ} -> /A11
- J5 pad 13: /BA -> /A12
- J5 pad 14: /BS -> /A13
- J5 pad 15: /~{VMA} -> /A14
- J5 pad 17: /A14 -> GND
- J5 pad 18: /A13 -> -12V
- J5 pad 19: /A12 -> +12V
- J5 pad 2: /D7 -> /A1
- J5 pad 20: /A11 -> GND
- J5 pad 21: /A10 -> +3V3
- J5 pad 22: /A9 -> +3V3
- J5 pad 23: /A8 -> GND
- J5 pad 24: /A7 -> /D0
- J5 pad 25: /A6 -> /D1
- J5 pad 26: /A5 -> /D2
- J5 pad 27: /A4 -> /D3
- J5 pad 28: /A3 -> /D4
- J5 pad 29: /A2 -> /D5
- J5 pad 3: /D6 -> /A2
- J5 pad 30: /A1 -> /D6
- J5 pad 31: /A0 -> /D7
- J5 pad 33: /RESET -> +5V
- J5 pad 35: /~{RESET} -> GND
- J5 pad 36: +3V3 -> /E
- J5 pad 37: /E -> /Q
- J5 pad 38: -12V -> /~{VMA}
- J5 pad 39: /Q -> GND
- J5 pad 4: /D5 -> /A3
- J5 pad 40: +12V -> /R/~{W}
- J5 pad 41: GND -> /~{RD}
- J5 pad 43: /~{RD} -> /~{RAM_{oe}}
- J5 pad 44: /R/~{W} -> GND
- J5 pad 45: /~{RAM_{oe}} -> /~{CBLK}
- J5 pad 46: /MMU_{en} -> /~{IORQ}
- J5 pad 47: /~{MRDY} -> /~{MREQ}
- J5 pad 49: /~{BREQ} -> /~{MRDY}
- J5 pad 5: /D4 -> /A4
- J5 pad 50: /~{NMI} -> /~{BREQ}
- J5 pad 51: /CLK_{acia} -> GND
- J5 pad 52: /~{IRQ7} -> /BA
- J5 pad 53: /~{IRQ6} -> /BS
- J5 pad 54: /~{IRQ5} -> /SPARE
- J5 pad 55: /~{IRQ4} -> /~{RESET}
- J5 pad 56: /~{IRQ3} -> /~{NMI}
- J5 pad 57: /~{IRQ2} -> /~{IRQ}
- J5 pad 58: /~{IRQ1} -> /~{FIRQ}
- J5 pad 59: /~{IRQ0} -> GND
- J5 pad 6: /D3 -> /A5
- J5 pad 61: /CLK_{cpu} -> +5V
- J5 pad 7: /D2 -> /A6
- J5 pad 8: /D1 -> /A7
- J5 pad 9: /D0 -> /A8
- J6 pad 1: /~{IORQ} -> /A0
- J6 pad 10: /~{CBLK} -> /A9
- J6 pad 11: /USR0 -> /A10
- J6 pad 12: /~{MREQ} -> /A11
- J6 pad 13: /BA -> /A12
- J6 pad 14: /BS -> /A13
- J6 pad 15: /~{VMA} -> /A14
- J6 pad 17: /A14 -> GND
- J6 pad 18: /A13 -> -12V
- J6 pad 19: /A12 -> +12V
- J6 pad 2: /D7 -> /A1
- J6 pad 20: /A11 -> GND
- J6 pad 21: /A10 -> +3V3
- J6 pad 22: /A9 -> +3V3
- J6 pad 23: /A8 -> GND
- J6 pad 24: /A7 -> /D0
- J6 pad 25: /A6 -> /D1
- J6 pad 26: /A5 -> /D2
- J6 pad 27: /A4 -> /D3
- J6 pad 28: /A3 -> /D4
- J6 pad 29: /A2 -> /D5
- J6 pad 3: /D6 -> /A2
- J6 pad 30: /A1 -> /D6
- J6 pad 31: /A0 -> /D7
- J6 pad 33: /RESET -> +5V
- J6 pad 35: /~{RESET} -> GND
- J6 pad 36: +3V3 -> /E
- J6 pad 37: /E -> /Q
- J6 pad 38: -12V -> /~{VMA}
- J6 pad 39: /Q -> GND
- J6 pad 4: /D5 -> /A3
- J6 pad 40: +12V -> /R/~{W}
- J6 pad 41: GND -> /~{RD}
- J6 pad 43: /~{RD} -> /~{RAM_{oe}}
- J6 pad 44: /R/~{W} -> GND
- J6 pad 45: /~{RAM_{oe}} -> /~{CBLK}
- J6 pad 46: /MMU_{en} -> /~{IORQ}
- J6 pad 47: /~{MRDY} -> /~{MREQ}
- J6 pad 49: /~{BREQ} -> /~{MRDY}
- J6 pad 5: /D4 -> /A4
- J6 pad 50: /~{NMI} -> /~{BREQ}
- J6 pad 51: /CLK_{acia} -> GND
- J6 pad 52: /~{IRQ7} -> /BA
- J6 pad 53: /~{IRQ6} -> /BS
- J6 pad 54: /~{IRQ5} -> /SPARE
- J6 pad 55: /~{IRQ4} -> /~{RESET}
- J6 pad 56: /~{IRQ3} -> /~{NMI}
- J6 pad 57: /~{IRQ2} -> /~{IRQ}
- J6 pad 58: /~{IRQ1} -> /~{FIRQ}
- J6 pad 59: /~{IRQ0} -> GND
- J6 pad 6: /D3 -> /A5
- J6 pad 61: /CLK_{cpu} -> +5V
- J6 pad 7: /D2 -> /A6
- J6 pad 8: /D1 -> /A7
- J6 pad 9: /D0 -> /A8
- J7 pad 1: /~{IORQ} -> /A0
- J7 pad 10: /~{CBLK} -> /A9
- J7 pad 11: /USR0 -> /A10
- J7 pad 12: /~{MREQ} -> /A11
- J7 pad 13: /BA -> /A12
- J7 pad 14: /BS -> /A13
- J7 pad 15: /~{VMA} -> /A14
- J7 pad 17: /A14 -> GND
- J7 pad 18: /A13 -> -12V
- J7 pad 19: /A12 -> +12V
- J7 pad 2: /D7 -> /A1
- J7 pad 20: /A11 -> GND
- J7 pad 21: /A10 -> +3V3
- J7 pad 22: /A9 -> +3V3
- J7 pad 23: /A8 -> GND
- J7 pad 24: /A7 -> /D0
- J7 pad 25: /A6 -> /D1
- J7 pad 26: /A5 -> /D2
- J7 pad 27: /A4 -> /D3
- J7 pad 28: /A3 -> /D4
- J7 pad 29: /A2 -> /D5
- J7 pad 3: /D6 -> /A2
- J7 pad 30: /A1 -> /D6
- J7 pad 31: /A0 -> /D7
- J7 pad 33: /RESET -> +5V
- J7 pad 35: /~{RESET} -> GND
- J7 pad 36: +3V3 -> /E
- J7 pad 37: /E -> /Q
- J7 pad 38: -12V -> /~{VMA}
- J7 pad 39: /Q -> GND
- J7 pad 4: /D5 -> /A3
- J7 pad 40: +12V -> /R/~{W}
- J7 pad 41: GND -> /~{RD}
- J7 pad 43: /~{RD} -> /~{RAM_{oe}}
- J7 pad 44: /R/~{W} -> GND
- J7 pad 45: /~{RAM_{oe}} -> /~{CBLK}
- J7 pad 46: /MMU_{en} -> /~{IORQ}
- J7 pad 47: /~{MRDY} -> /~{MREQ}
- J7 pad 49: /~{BREQ} -> /~{MRDY}
- J7 pad 5: /D4 -> /A4
- J7 pad 50: /~{NMI} -> /~{BREQ}
- J7 pad 51: /CLK_{acia} -> GND
- J7 pad 52: /~{IRQ7} -> /BA
- J7 pad 53: /~{IRQ6} -> /BS
- J7 pad 54: /~{IRQ5} -> /SPARE
- J7 pad 55: /~{IRQ4} -> /~{RESET}
- J7 pad 56: /~{IRQ3} -> /~{NMI}
- J7 pad 57: /~{IRQ2} -> /~{IRQ}
- J7 pad 58: /~{IRQ1} -> /~{FIRQ}
- J7 pad 59: /~{IRQ0} -> GND
- J7 pad 6: /D3 -> /A5
- J7 pad 61: /CLK_{cpu} -> +5V
- J7 pad 7: /D2 -> /A6
- J7 pad 8: /D1 -> /A7
- J7 pad 9: /D0 -> /A8
- J9 pad 1: /CLK_{1} -> /A0
- J9 pad 10: /~{IRQ12} -> /A9
- J9 pad 11: /A19 -> /A10
- J9 pad 12: /~{IRQ13} -> /A11
- J9 pad 13: /A18 -> /A12
- J9 pad 14: /~{IRQ14} -> /A13
- J9 pad 15: /A17 -> /A14
- J9 pad 16: /~{IRQ15} -> /A15
- J9 pad 17: /A16 -> GND
- J9 pad 18: /USR1 -> -12V
- J9 pad 19: /CLK_{2} -> +12V
- J9 pad 2: /~{IRQ8} -> /A1
- J9 pad 20: /USR2 -> GND
- J9 pad 21: /D8 -> +3V3
- J9 pad 22: /USR3 -> +3V3
- J9 pad 23: /D9 -> GND
- J9 pad 24: /USR4 -> /D0
- J9 pad 25: /D10 -> /D1
- J9 pad 26: /USR5 -> /D2
- J9 pad 27: /D11 -> /D3
- J9 pad 28: /USR6 -> /D4
- J9 pad 29: /D12 -> /D5
- J9 pad 3: /A23 -> /A2
- J9 pad 30: /USR7 -> /D6
- J9 pad 31: /D13 -> /D7
- J9 pad 32: +5V -> GND
- J9 pad 33: /D14 -> +5V
- J9 pad 34: /USR8 -> +5V
- J9 pad 35: /D15 -> GND
- J9 pad 36: GND -> /E
- J9 pad 4: /~{IRQ9} -> /A3
- J9 pad 5: /A22 -> /A4
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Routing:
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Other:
- board size 175.3 x 181.6 mm -> 282.6 x 120.7 mm
- board text added: "+12V"
- board text added: "+3V3"
- board text added: "-12V"
- board text added: "GND"
